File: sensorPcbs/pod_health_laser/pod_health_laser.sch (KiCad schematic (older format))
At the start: 2 parts, among them J1 RJ45, U1 laser_sensor

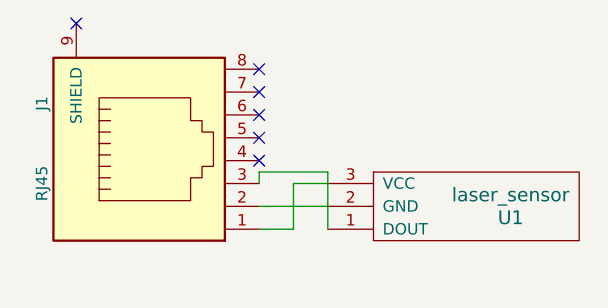
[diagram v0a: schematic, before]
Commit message: changed all the sensor PCB schematics and added the global component schematic library into each project
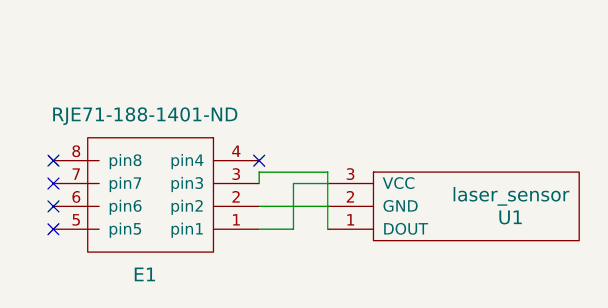
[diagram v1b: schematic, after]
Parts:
- removed J1: RJ45, Connectors:RJ45_8, symbol RJ45
- added E1: RJE71-188-1401-ND, symbol RJE71-188-1401-ND
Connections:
- net at U1.3 (VCC): now also E1.1 (pin1)
- net at U1.2 (GND): now also E1.2 (pin2)
- net at U1.1 (DOUT): now also E1.3 (pin3)
- no-connect marks 6 -> 5
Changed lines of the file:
@@
 EESchema Schematic File Version 2
-LIBS:power
-LIBS:device
-LIBS:transistors
-LIBS:conn
-LIBS:linear
-LIBS:regul
-LIBS:74xx
-LIBS:cmos4000
-LIBS:adc-dac
-LIBS:memory
-LIBS:xilinx
-LIBS:microcontrollers
-LIBS:dsp
-LIBS:microchip
-LIBS:analog_switches
-LIBS:motorola
-LIBS:texas
-LIBS:intel
-LIBS:audio
-LIBS:interface
-LIBS:digital-audio
-LIBS:philips
-LIBS:display
-LIBS:cypress
-LIBS:siliconi
-LIBS:opto
-LIBS:atmel
-LIBS:contrib
-LIBS:valves
 LIBS:laser_sensor
+LIBS:customSchematics
 LIBS:pod_health_laser-cache
 EELAYER 25 0
@@
 Comment4 ""
 $EndDescr
-$Comp
-L RJ45 J1
-U 1 1 58DAC1B3
-P 3250 2900
-F 0 "J1" H 3450 3400 50  0000 C CNN
-F 1 "RJ45" H 3100 3400 50  0000 C CNN
-F 2 "Connectors:RJ45_8" H 3250 2900 50  0001 C CNN
-F 3 "" H 3250 2900 50  0001 C CNN
-	1    3250 2900
-	0    -1   -1   0
-$EndComp
-NoConn ~ 2900 2350
-NoConn ~ 3700 2550
-NoConn ~ 3700 2650
-NoConn ~ 3700 2750
-NoConn ~ 3700 2850
 NoConn ~ 3700 2950
 $Comp
@@
 Wire Wire Line
 	3700 3000 3700 3050
+$Comp
+L RJE71-188-1401-ND E1
+U 1 1 59711D5E
+P 3500 3250
+F 0 "E1" H 3800 3450 60  0000 C CNN
+F 1 "RJE71-188-1401-ND" H 3800 2750 60  0000 C CNN
+F 2 "" H 3500 3250 60  0001 C CNN
+F 3 "" H 3500 3250 60  0001 C CNN
+	1    3500 3250
+	-1   0    0    1
+$EndComp
+NoConn ~ 2800 2950
+NoConn ~ 2800 3050
+NoConn ~ 2800 3150
+NoConn ~ 2800 3250
 $EndSCHEMATC

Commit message: added all the ferkin new ethernet shields to the sensor pcbs
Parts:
- E1: footprint (none) -> footprints:RJE71-188-1401-ND
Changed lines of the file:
@@
 F 0 "E1" H 3800 3450 60  0000 C CNN
 F 1 "RJE71-188-1401-ND" H 3800 2750 60  0000 C CNN
-F 2 "" H 3500 3250 60  0001 C CNN
+F 2 "footprints:RJE71-188-1401-ND" H 3500 3250 60  0001 C CNN
 F 3 "" H 3500 3250 60  0001 C CNN
 	1    3500 3250

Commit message: fixed the laser circuit
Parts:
- U1: footprint laser_sensor:laser_sensor -> laser_sensor:laser_sensor_new
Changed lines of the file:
@@
 EESchema Schematic File Version 2
+LIBS:power
+LIBS:device
+LIBS:transistors
+LIBS:conn
+LIBS:linear
+LIBS:regul
+LIBS:74xx
+LIBS:cmos4000
+LIBS:adc-dac
+LIBS:memory
+LIBS:xilinx
+LIBS:microcontrollers
+LIBS:dsp
+LIBS:microchip
+LIBS:analog_switches
+LIBS:motorola
+LIBS:texas
+LIBS:intel
+LIBS:audio
+LIBS:interface
+LIBS:digital-audio
+LIBS:philips
+LIBS:display
+LIBS:cypress
+LIBS:siliconi
+LIBS:opto
+LIBS:atmel
+LIBS:contrib
+LIBS:valves
 LIBS:laser_sensor
 LIBS:customSchematics
@@
 F 0 "U1" H 4800 3100 60  0000 C CNN
 F 1 "laser_sensor" H 4800 3200 60  0000 C CNN
-F 2 "laser_sensor:laser_sensor" H 4000 3150 60  0001 C CNN
+F 2 "laser_sensor:laser_sensor_new" H 4000 3150 60  0001 C CNN
 F 3 "" H 4000 3150 60  0001 C CNN
 	1    4000 3150
